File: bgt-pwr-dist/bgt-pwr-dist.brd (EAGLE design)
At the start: 40 x 100 mm, 32 parts

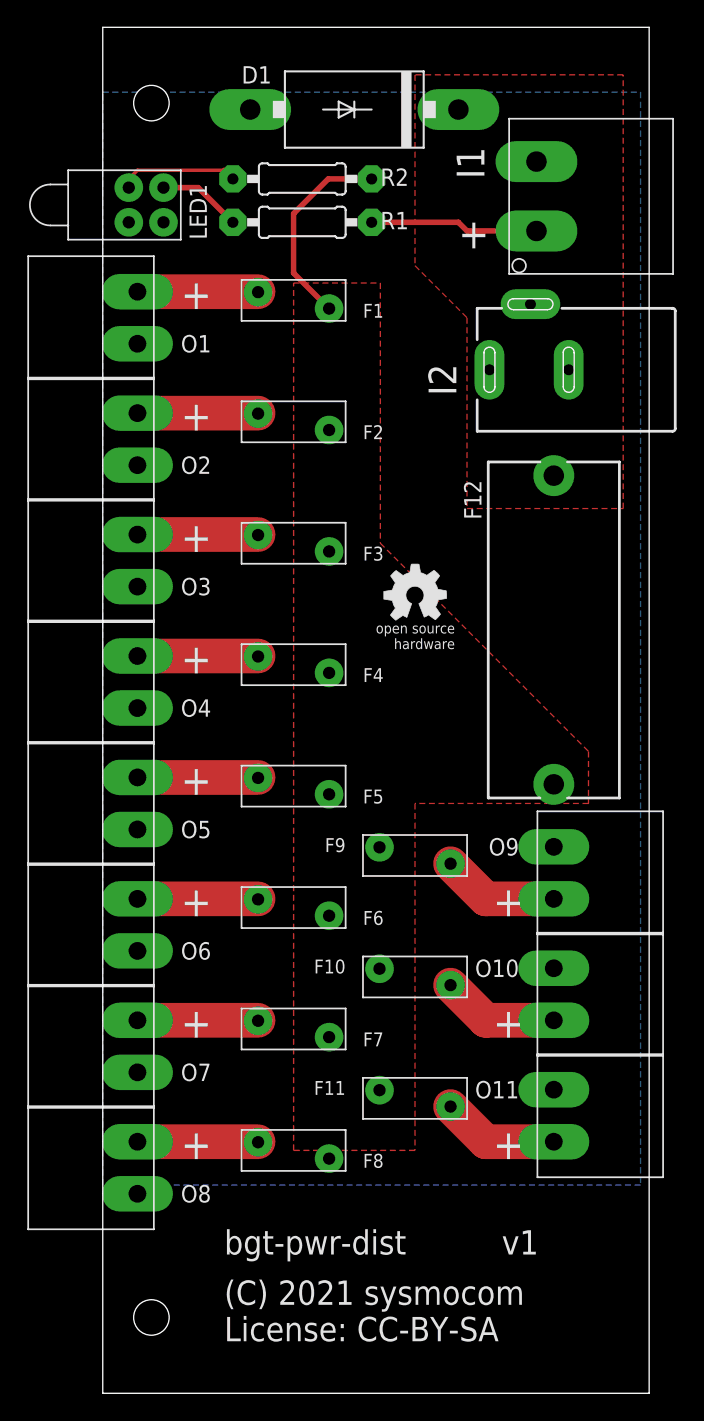
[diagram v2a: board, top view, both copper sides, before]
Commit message: bgt-pwr-dist: Finalize v2
* no milling for DC jack (cheaper PCB production)
* update version to v2
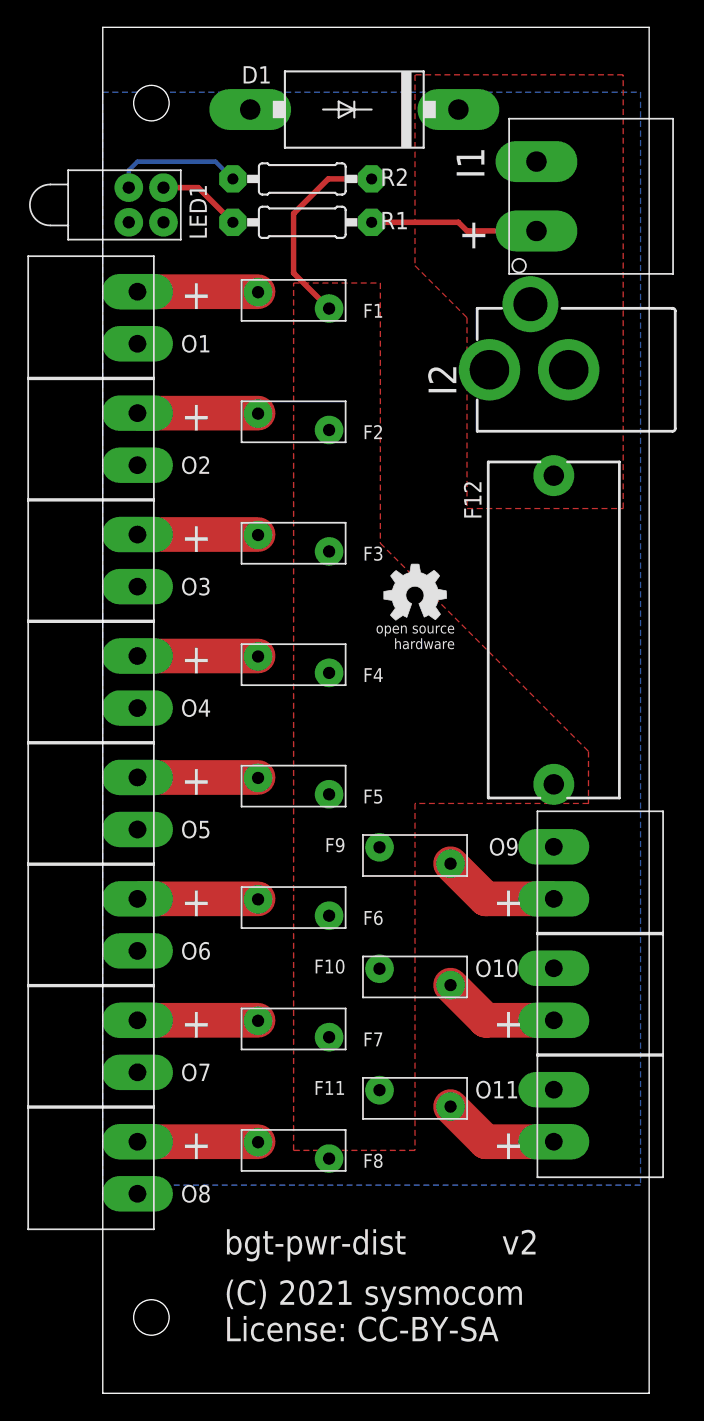
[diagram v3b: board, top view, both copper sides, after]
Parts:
- I2: value 694108301002 -> 694108301002-ROUND; device Wurth_Elektronik_Electromechanic_DC_Power_Jack_Connectors_rev15c:694108301002 -> Wurth_Elektronik_Electromechanic_DC_Power_Jack_Connectors_rev15c:694108301002_ROUND
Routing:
- net N$14: track 8.78 -> 9.68 mm
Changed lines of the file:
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@@
 </plain>
 <attributes>
-<attribute name="VERSION" value="v1"/>
+<attribute name="VERSION" value="v2"/>
 </attributes>
 <variantdefs>
@@
 <param name="mtCopper" value="0.035mm 0.035mm 0.035mm 0.035mm 0.035mm 0.035mm 0.035mm 0.035mm 0.035mm 0.035mm 0.035mm 0.035mm 0.035mm 0.035mm 0.035mm 0.035mm"/>
 <param name="mtIsolate" value="1.5mm 0.15mm 0.2mm 0.15mm 0.2mm 0.15mm 0.2mm 0.15mm 0.2mm 0.15mm 0.2mm 0.15mm 0.2mm 0.15mm 0.2mm"/>
-<param name="mdWireWire" value="8mil"/>
-<param name="mdWirePad" value="8mil"/>
-<param name="mdWireVia" value="8mil"/>
-<param name="mdPadPad" value="8mil"/>
-<param name="mdPadVia" value="8mil"/>
-<param name="mdViaVia" value="8mil"/>
-<param name="mdSmdPad" value="8mil"/>
-<param name="mdSmdVia" value="8mil"/>
-<param name="mdSmdSmd" value="8mil"/>
+<param name="mdWireWire" value="0.15mm"/>
+<param name="mdWirePad" value="0.15mm"/>
+<param name="mdWireVia" value="0.15mm"/>
+<param name="mdPadPad" value="0.15mm"/>
+<param name="mdPadVia" value="0.15mm"/>
+<param name="mdViaVia" value="0.15mm"/>
+<param name="mdSmdPad" value="0.15mm"/>
+<param name="mdSmdVia" value="0.15mm"/>
+<param name="mdSmdSmd" value="0.15mm"/>
 <param name="mdViaViaSameLayer" value="8mil"/>
 <param name="mnLayersViaInSmd" value="2"/>
-<param name="mdCopperDimension" value="40mil"/>
-<param name="mdDrill" value="8mil"/>
+<param name="mdCopperDimension" value="0.3mm"/>
+<param name="mdDrill" value="0.3mm"/>
 <param name="mdSmdStop" value="0mil"/>
-<param name="msWidth" value="10mil"/>
-<param name="msDrill" value="24mil"/>
+<param name="msWidth" value="0.2mm"/>
+<param name="msDrill" value="0.3mm"/>
 <param name="msMicroVia" value="9.99mm"/>
 <param name="msBlindViaRatio" value="0.5"/>
@@
 <attribute name="VALUE" x="30.48" y="93.98" size="1.27" layer="27"/>
 </element>
-<element name="I2" library="Wurth_Elektronik_Electromechanic_DC_Power_Jack_Connectors_rev15c" package="694108301002" value="694108301002" x="41.91" y="74.93" smashed="yes">
+<element name="I2" library="Wurth_Elektronik_Electromechanic_DC_Power_Jack_Connectors_rev15c" package="694108301002_ROUND" value="694108301002-ROUND" x="41.91" y="74.93" smashed="yes">
 <attribute name="NAME" x="25.885" y="73.03" size="2.032" layer="25" font="vector" ratio="13" rot="SR90"/>
 </element>
@@
 <contactref element="LED1" pad="4"/>
 <contactref element="R2" pad="1"/>
-<wire x1="1.905" y1="88.265" x2="1.905" y2="88.9" width="0.4064" layer="1"/>
-<wire x1="1.905" y1="88.9" x2="2.54" y2="89.535" width="0.254" layer="1"/>
-<wire x1="2.54" y1="89.535" x2="8.89" y2="89.535" width="0.254" layer="1"/>
-<wire x1="8.89" y1="89.535" x2="9.525" y2="88.9" width="0.4064" layer="1"/>
+<wire x1="1.905" y1="88.265" x2="1.905" y2="89.535" width="0.3048" layer="16"/>
+<wire x1="1.905" y1="89.535" x2="2.54" y2="90.17" width="0.3048" layer="16"/>
+<wire x1="2.54" y1="90.17" x2="8.255" y2="90.17" width="0.3048" layer="16"/>
+<wire x1="8.255" y1="90.17" x2="9.525" y2="88.9" width="0.3048" layer="16"/>
 </signal>
 </signals>

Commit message: bgt-pwr-dist: Part attribute annotation for BOM generation
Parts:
- F1, F10, F11, F2, F3, F4, F5, F6, F7, F8, F9: value (none) -> 3A
- R1, R2: value (none) -> 680
